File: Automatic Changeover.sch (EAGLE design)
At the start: 43 parts, among them IC1 ACS750LCA-050, IC2 XMEGA16A4A, IC3 XMEGA16A4A, IC4 ACS750LCA-050, IC5 ACS750LCA-050, K1 S216SE1, K2 S216SE1, K3 S216SE1, K4 S216SE1, K5 S216SE1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

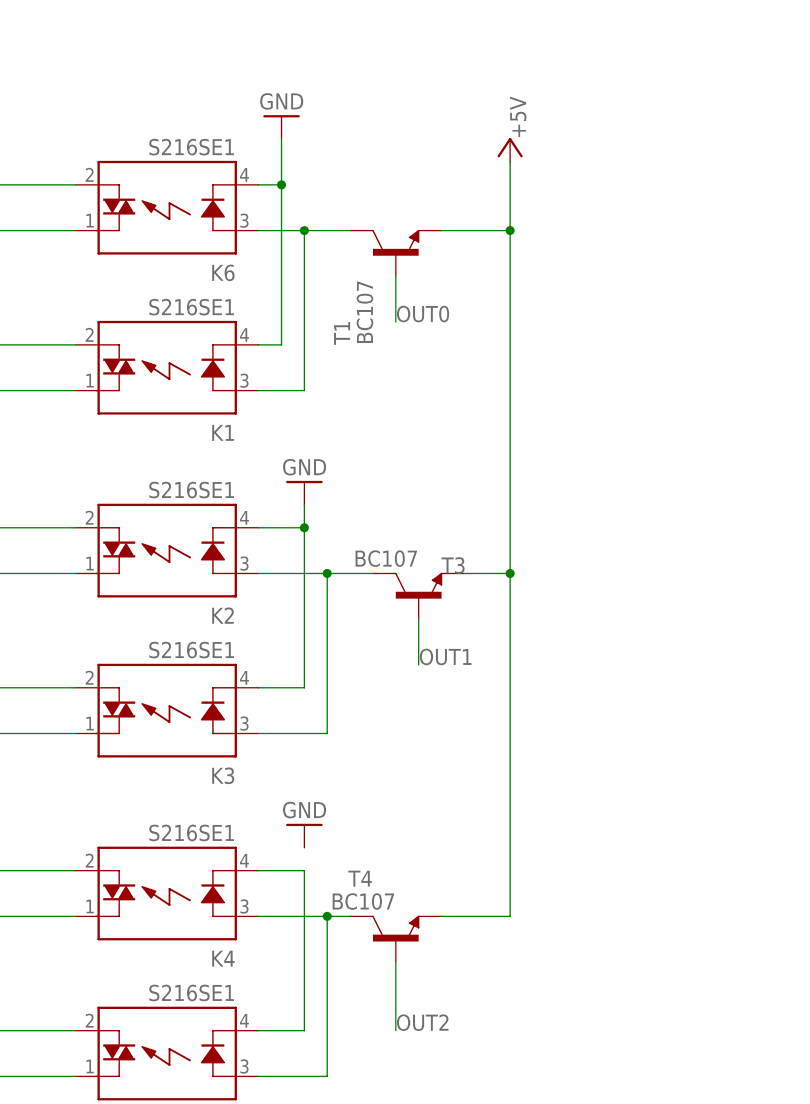
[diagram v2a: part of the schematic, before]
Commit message: completed polarity reversion of SSR relays
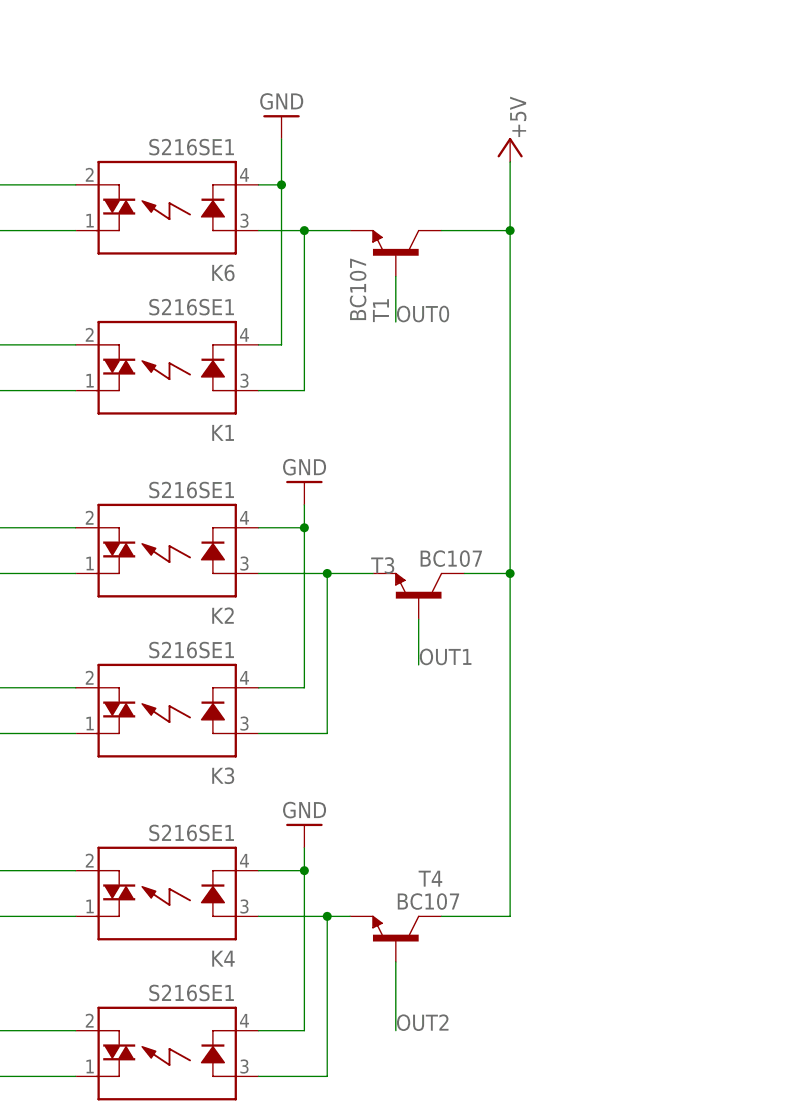
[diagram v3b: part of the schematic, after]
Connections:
- removed net N$3: K4.K, K5.K
- net +5V: now also T1.C, T3.C, T4.C; no longer T1.E, T3.E, T4.E
- net GND: now also K4.K, K5.K
- net N$58: now also T1.E; no longer T1.C
- net N$61: now also T3.E; no longer T3.C
- net N$63: now also T4.E; no longer T4.C
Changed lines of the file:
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@@
 <attribute name="VALUE" x="-63.5" y="-5.08" size="1.778" layer="96" rot="MR90"/>
 </instance>
-<instance part="T1" gate="G$1" x="-76.2" y="-17.78" smashed="yes" rot="R90">
-<attribute name="NAME" x="-81.28" y="-27.94" size="1.778" layer="95" rot="R90"/>
-<attribute name="VALUE" x="-78.74" y="-27.94" size="1.778" layer="96" rot="R90"/>
-</instance>
-<instance part="T3" gate="G$1" x="-73.66" y="-55.88" smashed="yes" rot="R90">
-<attribute name="NAME" x="-71.12" y="-53.34" size="1.778" layer="95"/>
-<attribute name="VALUE" x="-73.66" y="-50.8" size="1.778" layer="96" rot="R180"/>
-</instance>
-<instance part="T4" gate="G$1" x="-76.2" y="-93.98" smashed="yes" rot="R90">
-<attribute name="NAME" x="-78.74" y="-86.36" size="1.778" layer="95" rot="R180"/>
-<attribute name="VALUE" x="-76.2" y="-88.9" size="1.778" layer="96" rot="R180"/>
+<instance part="T1" gate="G$1" x="-76.2" y="-17.78" smashed="yes" rot="MR90">
+<attribute name="NAME" x="-78.74" y="-25.4" size="1.778" layer="95" rot="MR90"/>
+<attribute name="VALUE" x="-81.28" y="-25.4" size="1.778" layer="96" rot="MR90"/>
+</instance>
+<instance part="T3" gate="G$1" x="-73.66" y="-55.88" smashed="yes" rot="MR90">
+<attribute name="NAME" x="-76.2" y="-53.34" size="1.778" layer="95" rot="MR0"/>
+<attribute name="VALUE" x="-73.66" y="-50.8" size="1.778" layer="96" rot="MR180"/>
+</instance>
+<instance part="T4" gate="G$1" x="-76.2" y="-93.98" smashed="yes" rot="MR90">
+<attribute name="NAME" x="-73.66" y="-86.36" size="1.778" layer="95" rot="MR180"/>
+<attribute name="VALUE" x="-76.2" y="-88.9" size="1.778" layer="96" rot="MR180"/>
 </instance>
 <instance part="GND12" gate="1" x="-86.36" y="-81.28" smashed="yes" rot="R180">
@@
 </segment>
 <segment>
-<pinref part="T1" gate="G$1" pin="E"/>
-<wire x1="-71.12" y1="-15.24" x2="-63.5" y2="-15.24" width="0.1524" layer="91"/>
+<wire x1="-63.5" y1="-7.62" x2="-63.5" y2="-15.24" width="0.1524" layer="91"/>
+<pinref part="P+9" gate="1" pin="+5V"/>
+<pinref part="T4" gate="G$1" pin="C"/>
 <wire x1="-63.5" y1="-15.24" x2="-63.5" y2="-53.34" width="0.1524" layer="91"/>
-<pinref part="T3" gate="G$1" pin="E"/>
+<wire x1="-63.5" y1="-53.34" x2="-63.5" y2="-91.44" width="0.1524" layer="91"/>
+<wire x1="-71.12" y1="-91.44" x2="-63.5" y2="-91.44" width="0.1524" layer="91"/>
+<pinref part="T3" gate="G$1" pin="C"/>
 <wire x1="-68.58" y1="-53.34" x2="-63.5" y2="-53.34" width="0.1524" layer="91"/>
 <junction x="-63.5" y="-53.34"/>
-<pinref part="T4" gate="G$1" pin="E"/>
-<wire x1="-63.5" y1="-53.34" x2="-63.5" y2="-91.44" width="0.1524" layer="91"/>
-<wire x1="-63.5" y1="-91.44" x2="-71.12" y2="-91.44" width="0.1524" layer="91"/>
-<pinref part="P+9" gate="1" pin="+5V"/>
-<wire x1="-63.5" y1="-15.24" x2="-63.5" y2="-7.62" width="0.1524" layer="91"/>
+<pinref part="T1" gate="G$1" pin="C"/>
+<wire x1="-71.12" y1="-15.24" x2="-63.5" y2="-15.24" width="0.1524" layer="91"/>
 <junction x="-63.5" y="-15.24"/>
 </segment>
@@
 <wire x1="-86.36" y1="-45.72" x2="-86.36" y2="-48.26" width="0.1524" layer="91"/>
 <junction x="-86.36" y="-48.26"/>
+</segment>
+<segment>
+<pinref part="K5" gate="1" pin="K"/>
+<wire x1="-91.44" y1="-104.14" x2="-86.36" y2="-104.14" width="0.1524" layer="91"/>
+<wire x1="-86.36" y1="-104.14" x2="-86.36" y2="-86.36" width="0.1524" layer="91"/>
+<pinref part="K4" gate="1" pin="K"/>
+<wire x1="-91.44" y1="-86.36" x2="-86.36" y2="-86.36" width="0.1524" layer="91"/>
+<pinref part="GND12" gate="1" pin="GND"/>
+<wire x1="-86.36" y1="-83.82" x2="-86.36" y2="-86.36" width="0.1524" layer="91"/>
+<junction x="-86.36" y="-86.36"/>
 </segment>
 </net>
@@
 <wire x1="-91.44" y1="-15.24" x2="-86.36" y2="-15.24" width="0.1524" layer="91"/>
 <pinref part="K1" gate="1" pin="A"/>
-<wire x1="-86.36" y1="-15.24" x2="-81.28" y2="-15.24" width="0.1524" layer="91"/>
 <wire x1="-91.44" y1="-33.02" x2="-86.36" y2="-33.02" width="0.1524" layer="91"/>
 <wire x1="-86.36" y1="-33.02" x2="-86.36" y2="-15.24" width="0.1524" layer="91"/>
+<pinref part="T1" gate="G$1" pin="E"/>
+<wire x1="-86.36" y1="-15.24" x2="-81.28" y2="-15.24" width="0.1524" layer="91"/>
 <junction x="-86.36" y="-15.24"/>
-<pinref part="T1" gate="G$1" pin="C"/>
 </segment>
 </net>
@@
 <wire x1="-91.44" y1="-53.34" x2="-83.82" y2="-53.34" width="0.1524" layer="91"/>
 <pinref part="K3" gate="1" pin="A"/>
-<wire x1="-83.82" y1="-53.34" x2="-78.74" y2="-53.34" width="0.1524" layer="91"/>
 <wire x1="-91.44" y1="-71.12" x2="-83.82" y2="-71.12" width="0.1524" layer="91"/>
 <wire x1="-83.82" y1="-71.12" x2="-83.82" y2="-53.34" width="0.1524" layer="91"/>
+<pinref part="T3" gate="G$1" pin="E"/>
+<wire x1="-83.82" y1="-53.34" x2="-78.74" y2="-53.34" width="0.1524" layer="91"/>
 <junction x="-83.82" y="-53.34"/>
-<pinref part="T3" gate="G$1" pin="C"/>
 </segment>
 </net>
@@
 <wire x1="-91.44" y1="-91.44" x2="-83.82" y2="-91.44" width="0.1524" layer="91"/>
 <pinref part="K5" gate="1" pin="A"/>
-<wire x1="-83.82" y1="-91.44" x2="-81.28" y2="-91.44" width="0.1524" layer="91"/>
 <wire x1="-91.44" y1="-109.22" x2="-83.82" y2="-109.22" width="0.1524" layer="91"/>
 <wire x1="-83.82" y1="-109.22" x2="-83.82" y2="-91.44" width="0.1524" layer="91"/>
+<pinref part="T4" gate="G$1" pin="E"/>
+<wire x1="-83.82" y1="-91.44" x2="-81.28" y2="-91.44" width="0.1524" layer="91"/>
 <junction x="-83.82" y="-91.44"/>
-<pinref part="T4" gate="G$1" pin="C"/>
 </segment>
 </net>
@@
 </segment>
 </net>
-<net name="N$3" class="0">
-<segment>
-<pinref part="K5" gate="1" pin="K"/>
-<wire x1="-91.44" y1="-104.14" x2="-86.36" y2="-104.14" width="0.1524" layer="91"/>
-<wire x1="-86.36" y1="-104.14" x2="-86.36" y2="-86.36" width="0.1524" layer="91"/>
-<pinref part="K4" gate="1" pin="K"/>
-<wire x1="-91.44" y1="-86.36" x2="-86.36" y2="-86.36" width="0.1524" layer="91"/>
-</segment>
-</net>
